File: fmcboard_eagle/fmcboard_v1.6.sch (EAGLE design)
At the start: 281 parts, among them IC1 OPA699ID, IC10 LM358, IC11 7805DT, IC12 SN74AUC2G66DCTR, IC13 SN74AUC2G66DCTR, IC14 SN74AUC2G66DCTR, IC15 SN74AUC2G66DCTR, IC16 DAC7578SPWR, IC17 SN74AUC2G66DCTR, IC18 SN74AUC2G66DCTR, IC19 SN74AUC2G66DCTR, IC2 DAC7578SPWR, IC20 SN74AUC2G66DCTR, IC21 74AUP2GU04GW, IC22 74AUP2GU04GW, IC23 74AUP2GU04GW, IC24 74AUP2GU04GW, IC25 MC7905ACD2TR4G, IC26 AMS1117-1.8, IC27 LM358, IC28 SN74AUC2G66DCTR, IC29 LM337KVURG3, IC3 LTC6229IMS8E#TRPBF, IC30 SN74AUC2G66DCTR, IC31 SN74AUC2G66DCTR, IC32 SN74AUC2G66DCTR, IC33 LTC6229IMS8E#TRPBF, IC34 74AUP2GU04GW, IC35 74AUP2GU04GW, IC4 OPA695IDR, IC5 LTC6229IMS8E#TRPBF, IC6 OPA695IDR, IC7 OPA699ID, IC8 LM358, IC9 LM358, J1 8pin, J12 4p-2.54, J13 4p-2.54, J2 ASP-134604-01, J3 4p-2.54, J4 4p-2.54, J5 4p-2.54, J6 4p-2.54, J7 4p-2.54, J8 4p-2.54

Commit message: move 1.65s to 1.6
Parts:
- removed C112, C113, C114, C115, C2, C40: 10uF, rcl:C-EUC0402K
- removed J4, J6, J7: 4p-2.54, Seeed-Connector:DIP-BLACK-FEMALE-HEADER-VERT(4P-2.54)
- removed PULSESUMOUT: BU-SMB-V, con-coax:BU-SMB-V
- added C11, C121, C8: 0.1uF, passives:CAPACITOR0402_CAP
- added C120, C64: 10uF, rcl:C-EUC0805
- added C122: 0.01uF, passives:CAPACITOR0402_CAP
- added C123, C124, C125: 100uF, rcl:C-EUC1206K
- added D1, D2: B340A, SparkFun-DiscreteSemi:DIODE-SCHOTTKY-B340A
- added IC36, IC37: TPS5430DDAR, TPS5430DDAR:TPS5430DDAR
- added J9: 2p-2.54, Seeed-Connector:DIP-BLACK-MALE-HEADER-VERT(2P-2.54)
- added L3, L4: 10uH, SparkFun-Passives:INDUCTORPWR
- added PULSESOUT: BU-SMB-V, con-coax:BU-SMB-V
- added R116, R117, R60, R84: 1k, passives:RESISTOR0402_RES
- added R118, R73: 10k, passives:RESISTOR0402_RES
- C1, C110, C111, C34, C38, C39, C41, C77, C86: device rcl:C-EUC0402K -> rcl:C-EUC0805
- C10, C100, C101, C102, C103, C104, C105, C116, C117, C12, C13, C14, C15, C16, C17, C18, C19, C20, C21, C22, C23, C24, C25, C26, C27, C28, C29, C3, C30, C31, C32, C33, C35, C36, C37, C4, C42, C43, C44, C45, C46, C47, C48, C49, C5, C50, C51, C52, C53, C54, C55, C56, C57, C58, C59, C6, C60, C61, C62, C63, C65, C66, C67, C68, C69, C7, C70, C71, C72, C73, C74, C75, C76, C78, C79, C81, C82, C83, C84, C85, C87, C88, C89, C9, C90, C91, C92, C93, C94, C95, C96, C97, C98, C99: device rcl:C-EUC0402K -> passives:CAPACITOR0402_CAP
- C106: value 10uF -> 0.1uF; device rcl:C-EUC0402K -> passives:CAPACITOR0402_CAP
- C107: value 10uF -> 0.01uF; device rcl:C-EUC0402K -> passives:CAPACITOR0402_CAP
- C108, C109: value 10uF -> 100uF; device rcl:C-EUC0402K -> rcl:C-EUC1206K
- J3: value 4p-2.54 -> 2p-2.54; device Seeed-Connector:DIP-BLACK-FEMALE-HEADER-VERT(4P-2.54) -> Seeed-Connector:DIP-BLACK-MALE-HEADER-VERT(2P-2.54)
- R1, R10, R100, R101, R102, R103, R104, R105, R106, R107, R108, R109, R11, R110, R111, R112, R113, R114, R115, R12, R14, R15, R16, R17, R18, R19, R2, R20, R21, R22, R23, R24, R25, R26, R27, R28, R29, R30, R31, R32, R33, R34, R35, R36, R37, R38, R39, R4, R40, R41, R42, R43, R44, R45, R46, R47, R48, R49, R5, R50, R51, R52, R53, R54, R55, R56, R57, R58, R59, R6, R61, R62, R63, R64, R65, R66, R67, R68, R69, R7, R70, R74, R75, R76, R77, R78, R79, R8, R80, R81, R82, R83, R85, R87, R90, R91, R92, R93, R94, R95, R96, R97, R98, R99: device rcl:R-US_R0402 -> passives:RESISTOR0402_RES
- R13, R3, R71, R72, R86, R88, R89: device rcl:R-US_R0402 -> passives:RESISTOR0402_RES; LCSC C17415 -> (none)
- R9: value 1-3k -> 1?-3?k; device resistor:R-US_R0805 -> rcl:R-US_R0805
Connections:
- removed net N$35: J13.P$2, R71.1
- removed net N$38: J13.P$4, R72.1
- new net ARVIN: ARDUINO_NANO1.VIN
- new net BOOT1: C122.1, IC37.BOOT
- new net BOOT2: C107.1, IC36.BOOT
- new net FB1: IC37.VSENSE, R60.2, R73.1
- new net FB2: IC36.VSENSE, R116.2, R118.1
- new net N$29: C120.1, C64.2
- new net N$36: J5.P$2, R72.1
- new net N$53: C123.1, C124.2
- new net N$54: R60.1, R84.2
- new net N$55: C108.1, C109.2
- new net N$56: R116.1, R117.2
- new net N$57: J13.P$4, R71.1
- new net SW1: C122.2, D1.C, IC37.PH, L3.1
- new net SW2: C107.2, D2.C, IC36.PH, L4.1
- new net VIN: C11.1, C64.1, C8.1, IC36.VIN, IC37.VIN, J9.2
- net 12V: now also J9.1; no longer J8.P$2, J8.P$3, J8.P$4
- net 1V8-: now also C125.1; no longer C106.1, C107.1, C108.1, C109.1, C110.1, C111.1, C112.1, C113.1, C114.1, C115.1
- net 3V3: now also J8.P$4; no longer J3.P$1, J3.P$2, J3.P$3, J3.P$4
- net C18: now also SV2.19
- net C19: now also SV2.20
- net C22: now also SV1.1
- net C23: now also SV1.2
- net GND: now also C106.1, C109.1, C11.2, C111.1, C120.2, C121.2, C123.2, C125.2, C8.2, D1.A, IC37.EP, IC37.GND, J13.P$2, J3.1, J3.2, L4.2, PULSESOUT.2, R118.2, R84.1; no longer C106.2, C107.2, C108.2, C109.2, C111.2, C112.2, C113.2, C114.2, C115.2, C2.2, C40.1, J4.P$1, J4.P$2, J4.P$3, J4.P$4, J5.P$2, PULSESUMOUT.2, SV2.19, SV2.20
- net OP1BUF: now also R72.2; no longer R89.2
- net PULSEOUT: now also PULSESOUT.1; no longer PULSESUMOUT.1
- net SCLIN: no longer SV1.1
- net SDAIN: no longer SV1.2
- net TRANSOUT: now also R89.2; no longer R72.2
- net VIN+: now also C121.1, C124.1, L3.2, R73.2
- net VIN+CLEAN: now also C110.1; no longer C2.1
- net VIN-: now also C106.2, C108.2, D2.A, IC36.EP, IC36.GND, R117.1
- net VIN-CLEAN: now also C111.2; no longer C40.2
- net VS+: now also J8.P$2; no longer J6.P$1, J6.P$2, J6.P$3, J6.P$4
- net VS-: now also J8.P$3; no longer J7.P$1, J7.P$2, J7.P$3, J7.P$4
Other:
- note added: "Vout = (R1/R2 +1) * 1.221 V = (10/2 + 1) * 1.221 V = 7.3 V"
- note removed: "10*10uF=100uF"

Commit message: tantalum 100uF
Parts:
- removed C108, C109, C123, C124: 100uF, rcl:C-EUC1206K
- added C2, C40: 100uF, SparkFun-Passives:CAP_POLSMD
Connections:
- removed net N$53: C123.1, C124.2
- removed net N$55: C108.1, C109.2
- net GND: now also C2.-, C40.+; no longer C109.1, C123.2
- net VIN+: now also C2.+; no longer C124.1
- net VIN-: now also C40.-; no longer C108.2
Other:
- moved on the sheet: R116, R117, R60, R84

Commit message: routed
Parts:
- added C108, C109, C112, C80: 10uF, rcl:C-EUC0805
- added C113: 0.1uF, passives:CAPACITOR0402_CAP
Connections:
- new net N$35: C108.1, C80.2
- new net N$53: C109.1, C112.2
- net GND: now also C108.2
- net VIN: now also C112.1, C113.1, C80.1
- net VIN-: now also C109.2, C113.2

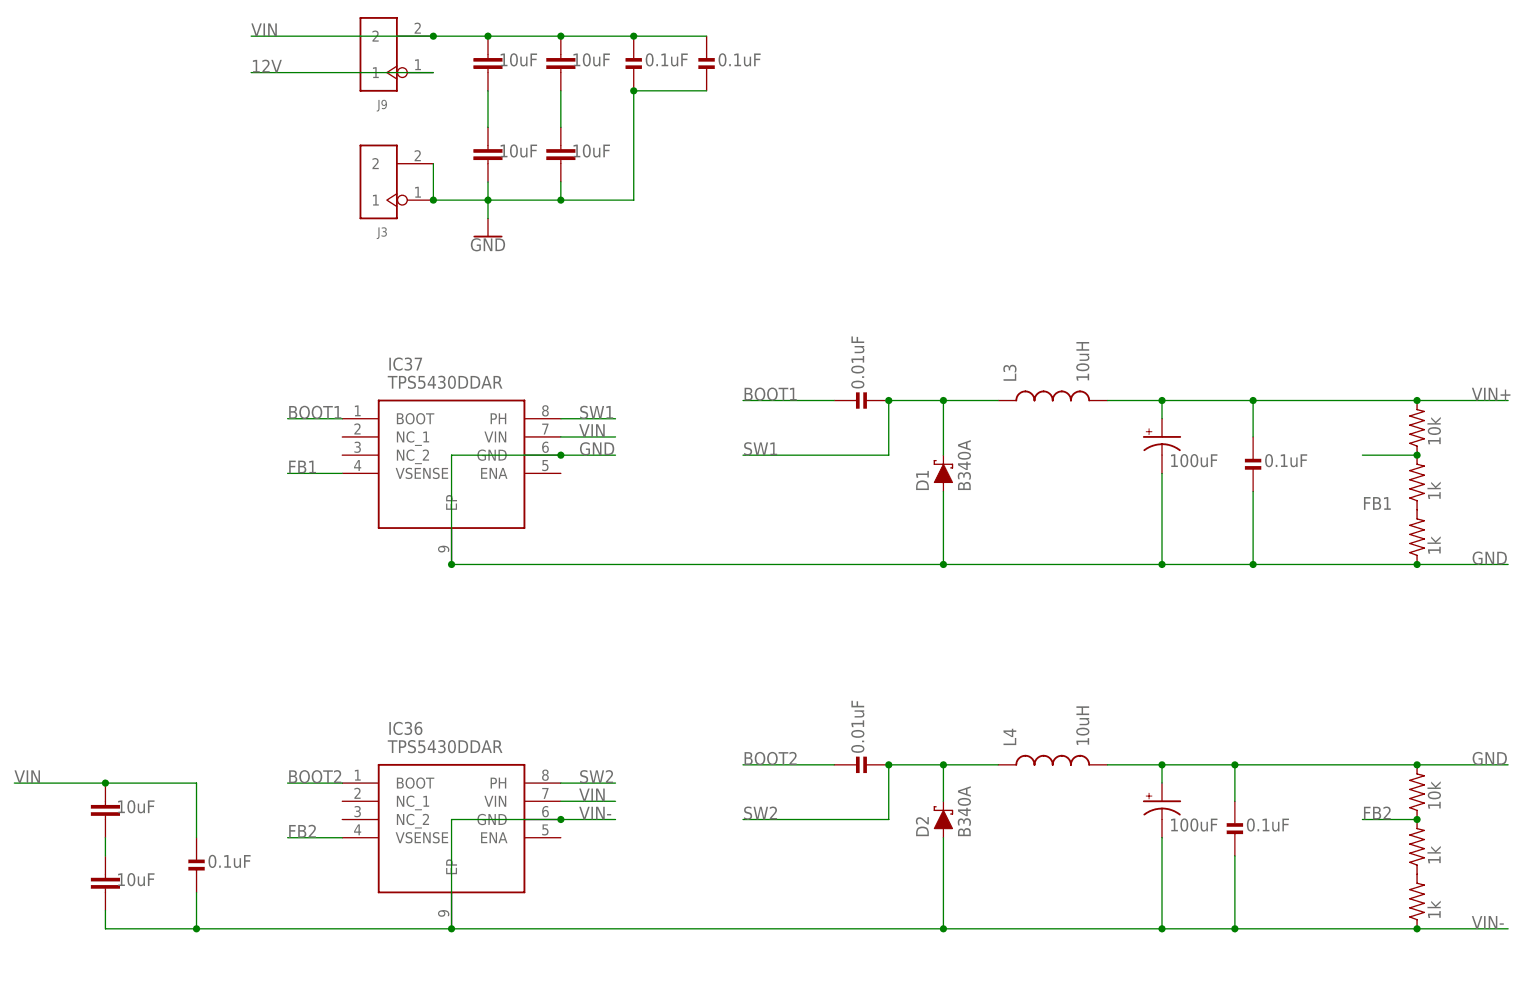
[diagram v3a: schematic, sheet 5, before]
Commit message: 0805 25V caps for 12V And double them for Vin to Vin- (12V+7V)
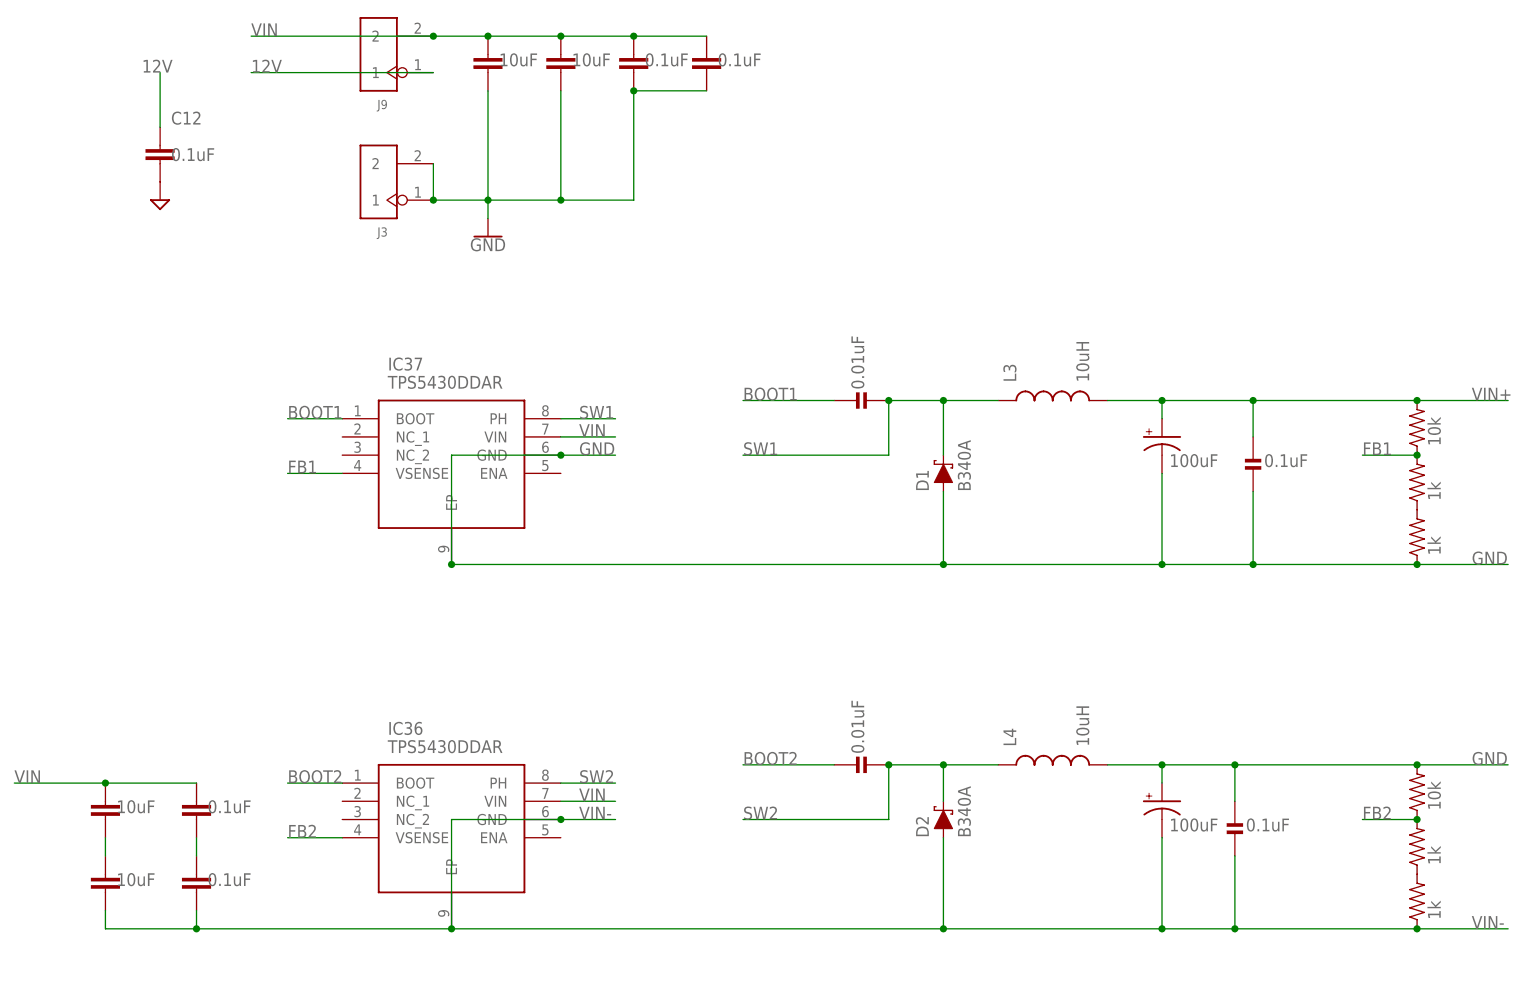
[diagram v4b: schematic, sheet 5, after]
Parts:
- removed C120: 10uF, rcl:C-EUC0805
- C108: value 10uF -> 0.1uF; device rcl:C-EUC0805 -> rcl:C-EUC0805K
- C11, C113, C12, C8: device passives:CAPACITOR0402_CAP -> rcl:C-EUC0805K
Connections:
- removed net N$29: C120.1, C64.2
- removed net N$35: C108.1, C80.2
- new net N$38: C108.2, C113.1
- net GND: now also C64.2, C80.2; no longer C108.2, C120.2
- net VIN: now also C108.1; no longer C113.1
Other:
- note added: "Caps rated for 25V"
- note added: "Caps rated for 25V Handling 12V+7V=19V, so double them"
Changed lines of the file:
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@@
 <part name="C9" library="passives" deviceset="CAPACITOR" device="0402_CAP" value="0.1uF"/>
 <part name="C10" library="passives" deviceset="CAPACITOR" device="0402_CAP" value="0.1uF"/>
-<part name="C12" library="passives" deviceset="CAPACITOR" device="0402_CAP" value="0.1uF"/>
+<part name="C12" library="rcl" library_urn="urn:adsk.eagle:library:334" deviceset="C-EU" device="C0805K" package3d_urn="urn:adsk.eagle:package:23681/2" value="0.1uF"/>
 <part name="C13" library="passives" deviceset="CAPACITOR" device="0402_CAP" value="0.1uF"/>
 <part name="C14" library="passives" deviceset="CAPACITOR" device="0402_CAP" value="0.1uF"/>
@@
 <part name="IC36" library="TPS5430DDAR" deviceset="TPS5430DDAR" device=""/>
 <part name="IC37" library="TPS5430DDAR" deviceset="TPS5430DDAR" device=""/>
-<part name="C120" library="rcl" library_urn="urn:adsk.eagle:library:334" deviceset="C-EU" device="C0805" package3d_urn="urn:adsk.eagle:package:23617/2" value="10uF"/>
 <part name="J3" library="Seeed-Connector" library_urn="urn:adsk.eagle:library:478" deviceset="DIP-BLACK-MALE-HEADER-VERT(2P-2.54)" device="" package3d_urn="urn:adsk.eagle:package:33132/1" value="2p-2.54"/>
 <part name="L3" library="SparkFun-Passives" deviceset="INDUCTOR" device="PWR" value="10uH">
@@
 <attribute name="LCSC" value="C7230"/>
 </part>
-<part name="C8" library="passives" deviceset="CAPACITOR" device="0402_CAP" value="0.1uF"/>
-<part name="C11" library="passives" deviceset="CAPACITOR" device="0402_CAP" value="0.1uF"/>
+<part name="C8" library="rcl" library_urn="urn:adsk.eagle:library:334" deviceset="C-EU" device="C0805K" package3d_urn="urn:adsk.eagle:package:23681/2" value="0.1uF"/>
+<part name="C11" library="rcl" library_urn="urn:adsk.eagle:library:334" deviceset="C-EU" device="C0805K" package3d_urn="urn:adsk.eagle:package:23681/2" value="0.1uF"/>
 <part name="C80" library="rcl" library_urn="urn:adsk.eagle:library:334" deviceset="C-EU" device="C0805" package3d_urn="urn:adsk.eagle:package:23617/2" value="10uF"/>
-<part name="C108" library="rcl" library_urn="urn:adsk.eagle:library:334" deviceset="C-EU" device="C0805" package3d_urn="urn:adsk.eagle:package:23617/2" value="10uF"/>
 <part name="C109" library="rcl" library_urn="urn:adsk.eagle:library:334" deviceset="C-EU" device="C0805" package3d_urn="urn:adsk.eagle:package:23617/2" value="10uF"/>
 <part name="C112" library="rcl" library_urn="urn:adsk.eagle:library:334" deviceset="C-EU" device="C0805" package3d_urn="urn:adsk.eagle:package:23617/2" value="10uF"/>
-<part name="C113" library="passives" deviceset="CAPACITOR" device="0402_CAP" value="0.1uF"/>
+<part name="C113" library="rcl" library_urn="urn:adsk.eagle:library:334" deviceset="C-EU" device="C0805K" package3d_urn="urn:adsk.eagle:package:23681/2" value="0.1uF"/>
+<part name="C108" library="rcl" library_urn="urn:adsk.eagle:library:334" deviceset="C-EU" device="C0805K" package3d_urn="urn:adsk.eagle:package:23681/2" value="0.1uF"/>
 </parts>
 <sheets>
@@
 <attribute name="VALUE" x="87.884" y="28.321" size="1.778" layer="96"/>
 </instance>
-<instance part="C12" gate="G$1" x="96.52" y="5.08" smashed="yes">
-<attribute name="NAME" x="98.044" y="8.001" size="1.778" layer="95"/>
-<attribute name="VALUE" x="98.044" y="2.921" size="1.778" layer="96"/>
-</instance>
 <instance part="C13" gate="G$1" x="104.14" y="5.08" smashed="yes">
 <attribute name="NAME" x="105.664" y="8.001" size="1.778" layer="95"/>
@@
 <instance part="SUPPLY13" gate="GND" x="-2.54" y="66.04" smashed="yes"/>
 <instance part="SUPPLY14" gate="GND" x="-12.7" y="66.04" smashed="yes"/>
-<instance part="SUPPLY15" gate="GND" x="96.52" y="-2.54" smashed="yes"/>
 <instance part="SUPPLY16" gate="GND" x="104.14" y="-2.54" smashed="yes"/>
 <instance part="SUPPLY17" gate="GND" x="111.76" y="-2.54" smashed="yes"/>
@@
 </segment>
 <segment>
-<pinref part="C12" gate="G$1" pin="2"/>
-<pinref part="SUPPLY15" gate="GND" pin="GND"/>
-</segment>
-<segment>
 <pinref part="C13" gate="G$1" pin="2"/>
 <pinref part="SUPPLY16" gate="GND" pin="GND"/>
@@
 <net name="12V" class="1">
 <segment>
-<pinref part="C12" gate="G$1" pin="1"/>
-<wire x1="96.52" y1="7.62" x2="96.52" y2="15.24" width="0.1524" layer="91"/>
-<label x="93.98" y="15.24" size="1.778" layer="95"/>
-</segment>
-<segment>
 <pinref part="J8" gate="G$1" pin="P$1"/>
 <wire x1="139.7" y1="5.08" x2="132.08" y2="5.08" width="0.1524" layer="91"/>
@@
 <text x="142.24" y="27.94" size="1.778" layer="90">Vout = (R1/R2 +1) * 1.221 V
         = (10/2 + 1) * 1.221  V = 7.3 V</text>
+<text x="-35.56" y="-58.42" size="1.778" layer="90">Caps rated for 25V
+Handling 12V+7V=19V, so double them</text>
+<text x="68.58" y="55.88" size="1.778" layer="90">Caps rated for 25V</text>
 </plain>
 <instances>
@@
 <attribute name="VALUE" x="29.21" y="22.86" size="1.778" layer="96" align="center-left"/>
 </instance>
-<instance part="C120" gate="G$1" x="43.18" y="55.88" smashed="yes">
-<attribute name="VALUE" x="44.704" y="54.229" size="1.778" layer="96"/>
-</instance>
 <instance part="J3" gate="G$1" x="27.94" y="50.8" smashed="yes" rot="R180">
 <attribute name="NAME" x="29.21" y="44.45" size="1.27" layer="95" ratio="10" rot="R180"/>
@@
 <attribute name="VALUE" x="54.864" y="66.929" size="1.778" layer="96"/>
 </instance>
-<instance part="C108" gate="G$1" x="53.34" y="55.88" smashed="yes">
-<attribute name="VALUE" x="54.864" y="54.229" size="1.778" layer="96"/>
-</instance>
 <instance part="C109" gate="G$1" x="-10.16" y="-45.72" smashed="yes">
 <attribute name="VALUE" x="-8.636" y="-47.371" size="1.778" layer="96"/>
@@
 <attribute name="VALUE" x="-8.636" y="-37.211" size="1.778" layer="96"/>
 </instance>
-<instance part="C113" gate="G$1" x="2.54" y="-43.18" smashed="yes">
-<attribute name="VALUE" x="4.064" y="-44.831" size="1.778" layer="96"/>
+<instance part="C113" gate="G$1" x="2.54" y="-45.72" smashed="yes">
+<attribute name="VALUE" x="4.064" y="-47.371" size="1.778" layer="96"/>
+</instance>
+<instance part="C108" gate="G$1" x="2.54" y="-35.56" smashed="yes">
+<attribute name="VALUE" x="4.064" y="-37.211" size="1.778" layer="96"/>
 </instance>
+<instance part="C12" gate="G$1" x="-2.54" y="55.88" smashed="yes">
+<attribute name="NAME" x="-1.016" y="58.801" size="1.778" layer="95"/>
+<attribute name="VALUE" x="-1.016" y="53.721" size="1.778" layer="96"/>
+</instance>
+<instance part="SUPPLY15" gate="GND" x="-2.54" y="48.26" smashed="yes"/>
 </instances>
 <busses>
@@
 <pinref part="C112" gate="G$1" pin="1"/>
 <wire x1="-22.86" y1="-33.02" x2="-10.16" y2="-33.02" width="0.1524" layer="91"/>
+<label x="-22.86" y="-33.02" size="1.778" layer="95"/>
+<pinref part="C108" gate="G$1" pin="1"/>
 <wire x1="-10.16" y1="-33.02" x2="2.54" y2="-33.02" width="0.1524" layer="91"/>
 <junction x="-10.16" y="-33.02"/>
-<pinref part="C113" gate="G$1" pin="1"/>
-<wire x1="2.54" y1="-33.02" x2="2.54" y2="-40.64" width="0.1524" layer="91"/>
-<label x="-22.86" y="-33.02" size="1.778" layer="95"/>
 </segment>
 </net>
@@
 <pinref part="J3" gate="G$1" pin="2"/>
 <wire x1="35.56" y1="53.34" x2="35.56" y2="48.26" width="0.1524" layer="91"/>
-<pinref part="C120" gate="G$1" pin="2"/>
-<wire x1="43.18" y1="50.8" x2="43.18" y2="48.26" width="0.1524" layer="91"/>
 <pinref part="C11" gate="G$1" pin="2"/>
 <pinref part="C8" gate="G$1" pin="2"/>
@@
 <junction x="63.5" y="63.5"/>
 <wire x1="63.5" y1="48.26" x2="53.34" y2="48.26" width="0.1524" layer="91"/>
-<pinref part="C108" gate="G$1" pin="2"/>
 <wire x1="53.34" y1="48.26" x2="43.18" y2="48.26" width="0.1524" layer="91"/>
-<wire x1="53.34" y1="50.8" x2="53.34" y2="48.26" width="0.1524" layer="91"/>
 <junction x="53.34" y="48.26"/>
+<pinref part="C64" gate="G$1" pin="2"/>
+<wire x1="43.18" y1="48.26" x2="43.18" y2="63.5" width="0.1524" layer="91"/>
+<pinref part="C80" gate="G$1" pin="2"/>
+<wire x1="53.34" y1="48.26" x2="53.34" y2="63.5" width="0.1524" layer="91"/>
 </segment>
 <segment>
@@
 <junction x="137.16" y="-2.54"/>
 </segment>
+<segment>
+<pinref part="C12" gate="G$1" pin="2"/>
+<pinref part="SUPPLY15" gate="GND" pin="GND"/>
+</segment>
 </net>
 <net name="SW1" class="0">
@@
 </segment>
 <segment>
-<label x="165.1" y="5.08" size="1.778" layer="95"/>
+<label x="165.1" y="12.7" size="1.778" layer="95"/>
 <pinref part="R60" gate="G$1" pin="2"/>
 <wire x1="165.1" y1="12.7" x2="172.72" y2="12.7" width="0.1524" layer="91"/>
@@
 </segment>
 </net>
-<net name="N$29" class="0">
-<segment>
-<pinref part="C64" gate="G$1" pin="2"/>
-<pinref part="C120" gate="G$1" pin="1"/>
-<wire x1="43.18" y1="58.42" x2="43.18" y2="63.5" width="0.1524" layer="91"/>
-</segment>
-</net>
 <net name="12V" class="1">
 <segment>
@@
 <label x="10.16" y="66.04" size="1.778" layer="95"/>
 </segment>
+<segment>
+<pinref part="C12" gate="G$1" pin="1"/>
+<wire x1="-2.54" y1="58.42" x2="-2.54" y2="66.04" width="0.1524" layer="91"/>
+<label x="-5.08" y="66.04" size="1.778" layer="95"/>
+</segment>
 </net>
 <net name="VIN+" class="1">
@@
 <junction x="137.16" y="-53.34"/>
 <pinref part="C113" gate="G$1" pin="2"/>
-<wire x1="2.54" y1="-48.26" x2="2.54" y2="-53.34" width="0.1524" layer="91"/>
+<wire x1="2.54" y1="-50.8" x2="2.54" y2="-53.34" width="0.1524" layer="91"/>
 <wire x1="2.54" y1="-53.34" x2="38.1" y2="-53.34" width="0.1524" layer="91"/>
 <pinref part="C109" gate="G$1" pin="2"/>
@@
 </segment>
 </net>
-<net name="N$35" class="0">
-<segment>
-<pinref part="C80" gate="G$1" pin="2"/>
-<pinref part="C108" gate="G$1" pin="1"/>
-<wire x1="53.34" y1="63.5" x2="53.34" y2="58.42" width="0.1524" layer="91"/>
-</segment>
-</net>
 <net name="N$53" class="0">
 <segment>
@@
 </segment>
 </net>
+<net name="N$38" class="0">
+<segment>
+<pinref part="C108" gate="G$1" pin="2"/>
+<pinref part="C113" gate="G$1" pin="1"/>
+<wire x1="2.54" y1="-40.64" x2="2.54" y2="-43.18" width="0.1524" layer="91"/>
+</segment>
+</net>
